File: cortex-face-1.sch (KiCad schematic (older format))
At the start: 12 parts, among them U1 ProMicro

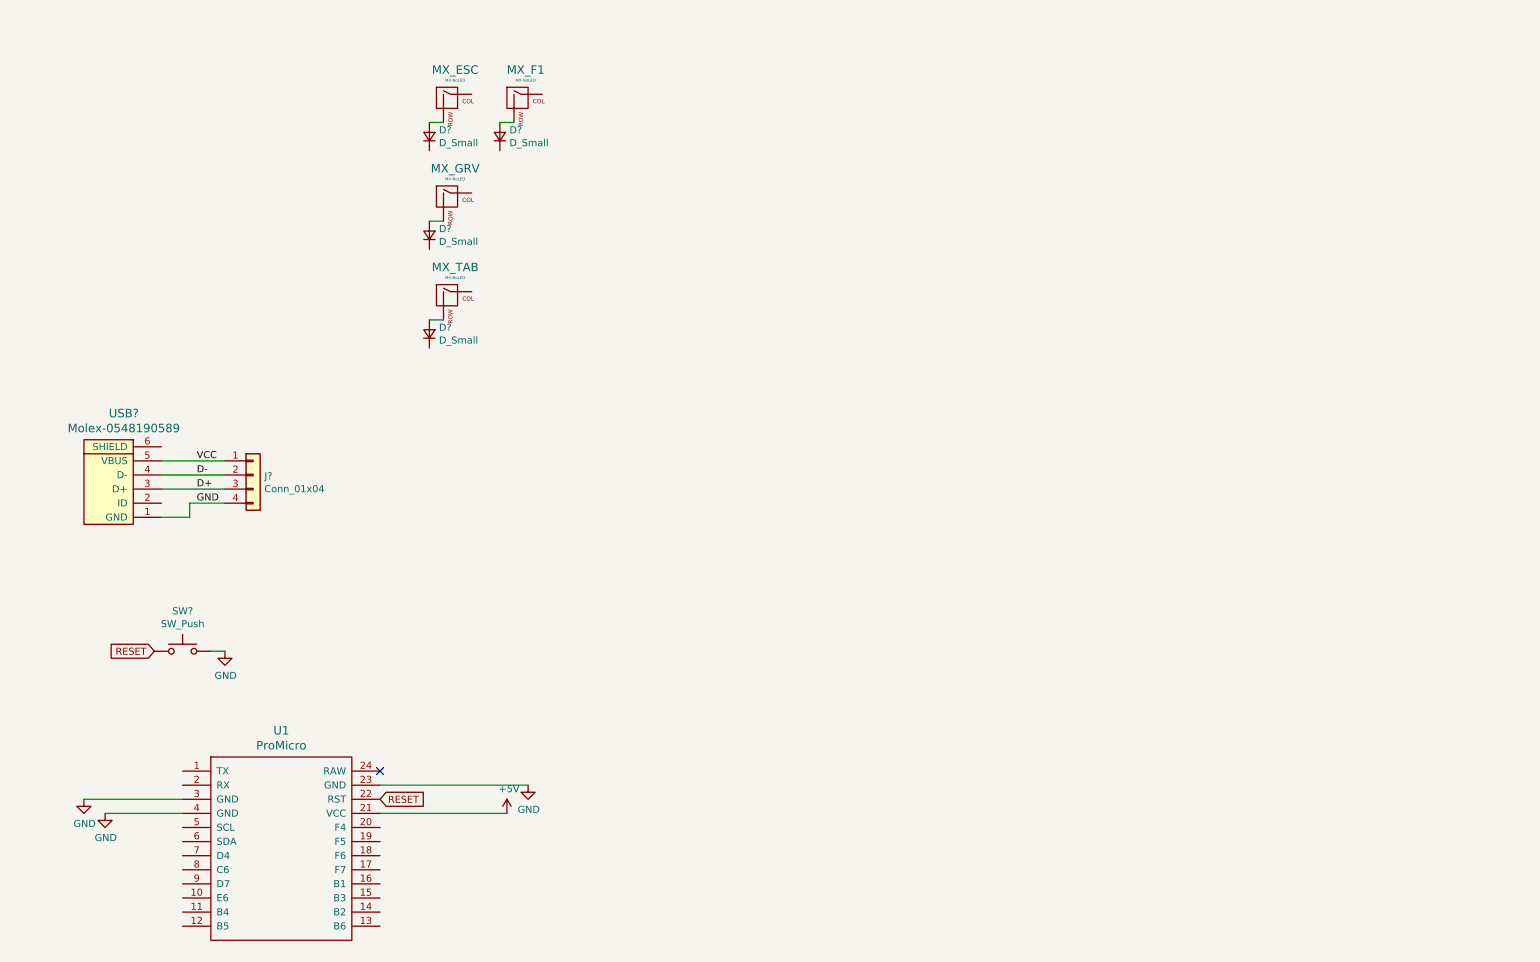
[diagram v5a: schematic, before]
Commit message: 10x9 layout
Changed switch matrix to 10x9 (columns x rows) to use fewer pins
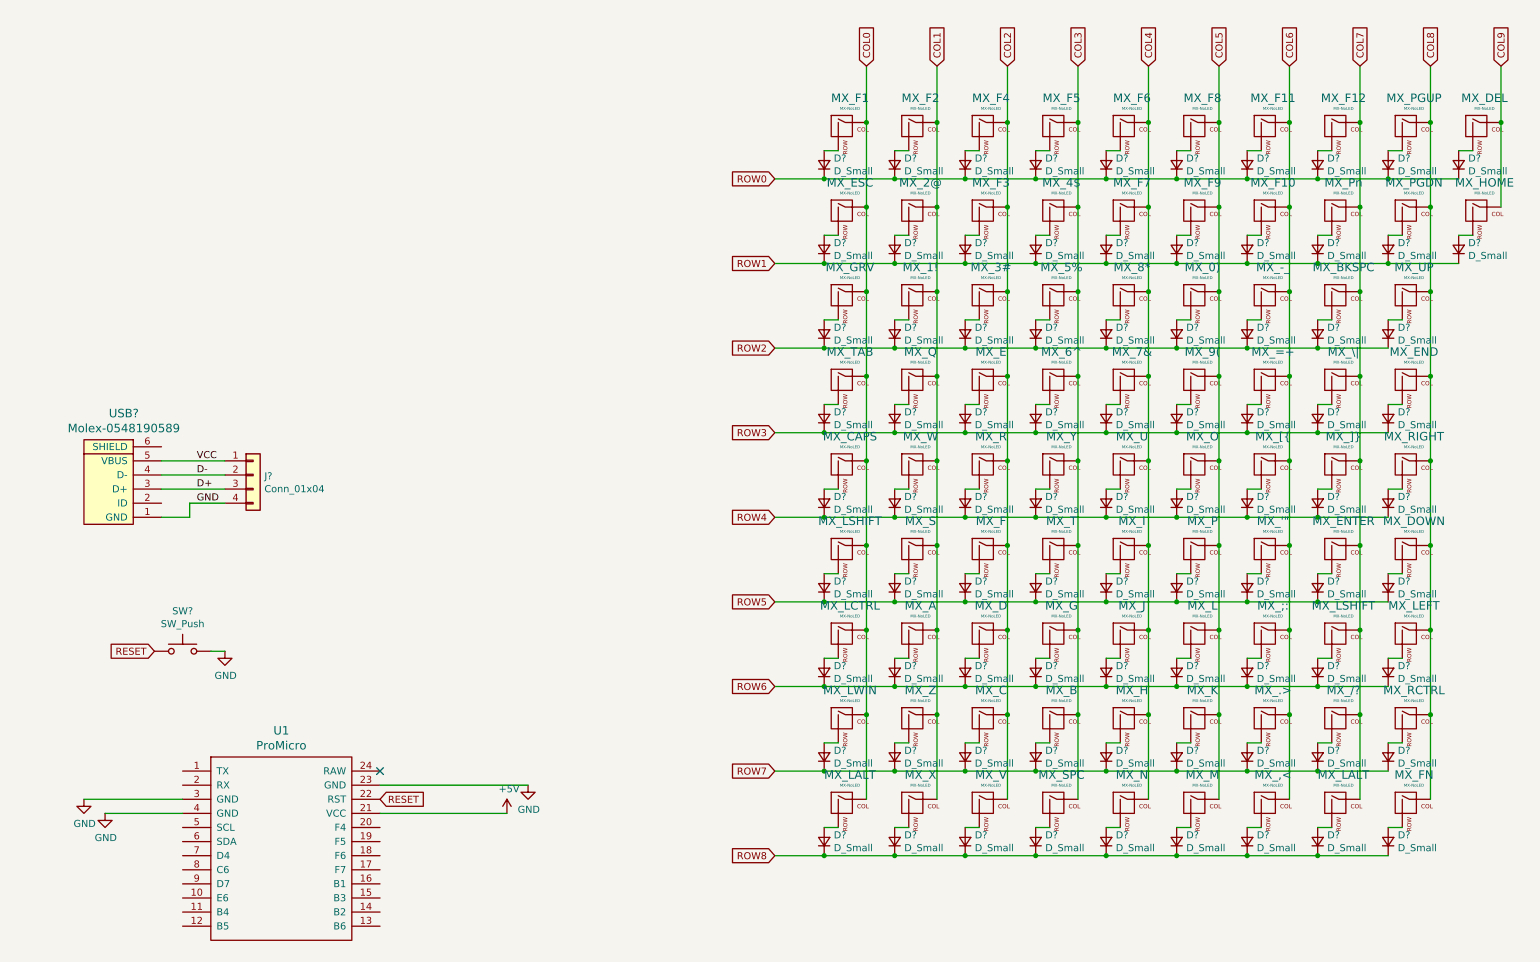
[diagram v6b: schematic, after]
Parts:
- added D? (x79): D_Small, symbol Device:D_Small
- added MX_'", MX_,<, MX_-_, MX_.>, MX_/?, MX_0), MX_1!, MX_2@, MX_3#, MX_4$, MX_5%, MX_6^, MX_7&, MX_8*, MX_9(, MX_;:, MX_=+, MX_A, MX_B, MX_BKSPC, MX_C, MX_CAPS, MX_D, MX_DEL, MX_DOWN, MX_E, MX_END, MX_ENTER, MX_F, MX_F10, MX_F11, MX_F12, MX_F2, MX_F3, MX_F4, MX_F5, MX_F6, MX_F7, MX_F8, MX_F9, MX_FN, MX_G, MX_H, MX_HOME, MX_I, MX_J, MX_K, MX_L, MX_LALT (x2), MX_LCTRL, MX_LEFT, MX_LSHIFT (x2), MX_LWIN, MX_M, MX_N, MX_O, MX_P, MX_PGDN, MX_PGUP, MX_Pn, MX_Q, MX_R, MX_RCTRL, MX_RIGHT, MX_S, MX_SPC, MX_T, MX_U, MX_UP, MX_V, MX_W, MX_X, MX_Y, MX_Z, MX_[{, MX_\|, MX_]}: MX-NoLED, symbol MX_Alps_Hybrid:MX-NoLED
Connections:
- net COL0: now reaches MX_F1.1 (COL)
- net COL0: now also MX_ESC.1 (COL), MX_GRV.1 (COL), MX_TAB.1 (COL), MX_CAPS.1 (COL), MX_LALT.1 (COL), MX_LCTRL.1 (COL), MX_LSHIFT.1 (COL), MX_LWIN.1 (COL)
- net ROW0: now reaches D?.1 (K)
- net ROW0: now also D?.1 (K), D?.1 (K), D?.1 (K), D?.1 (K), D?.1 (K), D?.1 (K), D?.1 (K), D?.1 (K), D?.1 (K)
- net ROW1: now reaches D?.1 (K)
- net ROW1: now also D?.1 (K), D?.1 (K), D?.1 (K), D?.1 (K), D?.1 (K), D?.1 (K), D?.1 (K), D?.1 (K), D?.1 (K)
- net ROW2: now reaches D?.1 (K)
- net ROW2: now also D?.1 (K), D?.1 (K), D?.1 (K), D?.1 (K), D?.1 (K), D?.1 (K), D?.1 (K), D?.1 (K)
- net ROW3: now reaches D?.1 (K)
- net ROW3: now also D?.1 (K), D?.1 (K), D?.1 (K), D?.1 (K), D?.1 (K), D?.1 (K), D?.1 (K), D?.1 (K)
- new net: D?.2 (A), MX_CAPS.2 (ROW)
- new net: D?.2 (A), MX_LSHIFT.2 (ROW) (x2)
- new net: D?.2 (A), MX_LCTRL.2 (ROW)
- new net: D?.2 (A), MX_LWIN.2 (ROW)
- new net: D?.2 (A), MX_LALT.2 (ROW) (x2)
- new net: D?.2 (A), MX_F2.2 (ROW)
- new net: D?.2 (A), MX_2@.2 (ROW)
- new net: D?.2 (A), MX_1!.2 (ROW)
- new net: D?.2 (A), MX_Q.2 (ROW)
- new net: D?.2 (A), MX_W.2 (ROW)
- new net: D?.2 (A), MX_S.2 (ROW)
- new net: D?.2 (A), MX_A.2 (ROW)
- new net: D?.2 (A), MX_Z.2 (ROW)
- new net: D?.2 (A), MX_X.2 (ROW)
- new net: D?.2 (A), MX_F4.2 (ROW)
- new net: D?.2 (A), MX_F3.2 (ROW)
- new net: D?.2 (A), MX_3#.2 (ROW)
- new net: D?.2 (A), MX_E.2 (ROW)
- new net: D?.2 (A), MX_R.2 (ROW)
- new net: D?.2 (A), MX_F.2 (ROW)
- new net: D?.2 (A), MX_D.2 (ROW)
- new net: D?.2 (A), MX_C.2 (ROW)
- new net: D?.2 (A), MX_V.2 (ROW)
- new net: D?.2 (A), MX_F5.2 (ROW)
- new net: D?.2 (A), MX_4$.2 (ROW)
- new net: D?.2 (A), MX_5%.2 (ROW)
- new net: D?.2 (A), MX_6^.2 (ROW)
- new net: D?.2 (A), MX_Y.2 (ROW)
- new net: D?.2 (A), MX_T.2 (ROW)
- new net: D?.2 (A), MX_G.2 (ROW)
- new net: D?.2 (A), MX_B.2 (ROW)
- new net: D?.2 (A), MX_SPC.2 (ROW)
- new net: D?.2 (A), MX_F6.2 (ROW)
- new net: D?.2 (A), MX_F7.2 (ROW)
- new net: D?.2 (A), MX_8*.2 (ROW)
- new net: D?.2 (A), MX_7&.2 (ROW)
- new net: D?.2 (A), MX_U.2 (ROW)
- new net: D?.2 (A), MX_I.2 (ROW)
- new net: D?.2 (A), MX_J.2 (ROW)
- new net: D?.2 (A), MX_H.2 (ROW)
- new net: D?.2 (A), MX_N.2 (ROW)
- new net: D?.2 (A), MX_F8.2 (ROW)
- new net: D?.2 (A), MX_F9.2 (ROW)
- new net: D?.2 (A), MX_0).2 (ROW)
- new net: D?.2 (A), MX_9(.2 (ROW)
- new net: D?.2 (A), MX_O.2 (ROW)
- new net: D?.2 (A), MX_P.2 (ROW)
- new net: D?.2 (A), MX_L.2 (ROW)
- new net: D?.2 (A), MX_K.2 (ROW)
- new net: D?.2 (A), MX_M.2 (ROW)
- new net: D?.2 (A), MX_F11.2 (ROW)
- new net: D?.2 (A), MX_F10.2 (ROW)
- new net: D?.2 (A), MX_-_.2 (ROW)
- new net: D?.2 (A), MX_=+.2 (ROW)
- new net: D?.2 (A), MX_[{.2 (ROW)
- new net: D?.2 (A), MX_'".2 (ROW)
- new net: D?.2 (A), MX_;:.2 (ROW)
- new net: D?.2 (A), MX_.>.2 (ROW)
- new net: D?.2 (A), MX_,<.2 (ROW)
- new net: D?.2 (A), MX_F12.2 (ROW)
- new net: D?.2 (A), MX_Pn.2 (ROW)
- new net: D?.2 (A), MX_BKSPC.2 (ROW)
- new net: D?.2 (A), MX_\|.2 (ROW)
- new net: D?.2 (A), MX_]}.2 (ROW)
- new net: D?.2 (A), MX_ENTER.2 (ROW)
- new net: D?.2 (A), MX_/?.2 (ROW)
- new net: D?.2 (A), MX_PGUP.2 (ROW)
- new net: D?.2 (A), MX_PGDN.2 (ROW)
- new net: D?.2 (A), MX_UP.2 (ROW)
- new net: D?.2 (A), MX_END.2 (ROW)
- new net: D?.2 (A), MX_RIGHT.2 (ROW)
- new net: D?.2 (A), MX_DOWN.2 (ROW)
- new net: D?.2 (A), MX_LEFT.2 (ROW)
- new net: D?.2 (A), MX_RCTRL.2 (ROW)
- new net: D?.2 (A), MX_FN.2 (ROW)
- new net: D?.2 (A), MX_DEL.2 (ROW)
- new net: D?.2 (A), MX_HOME.2 (ROW)
- new net COL1: MX_1!.1 (COL), MX_2@.1 (COL), MX_A.1 (COL), MX_F2.1 (COL), MX_Q.1 (COL), MX_S.1 (COL), MX_W.1 (COL), MX_X.1 (COL), MX_Z.1 (COL)
- new net COL2: MX_3#.1 (COL), MX_C.1 (COL), MX_D.1 (COL), MX_E.1 (COL), MX_F.1 (COL), MX_F3.1 (COL), MX_F4.1 (COL), MX_R.1 (COL), MX_V.1 (COL)
- new net COL3: MX_4$.1 (COL), MX_5%.1 (COL), MX_6^.1 (COL), MX_B.1 (COL), MX_F5.1 (COL), MX_G.1 (COL), MX_SPC.1 (COL), MX_T.1 (COL), MX_Y.1 (COL)
- new net COL4: MX_7&.1 (COL), MX_8*.1 (COL), MX_F6.1 (COL), MX_F7.1 (COL), MX_H.1 (COL), MX_I.1 (COL), MX_J.1 (COL), MX_N.1 (COL), MX_U.1 (COL)
- new net COL5: MX_0).1 (COL), MX_9(.1 (COL), MX_F8.1 (COL), MX_F9.1 (COL), MX_K.1 (COL), MX_L.1 (COL), MX_M.1 (COL), MX_O.1 (COL), MX_P.1 (COL)
- new net COL6: MX_'".1 (COL), MX_,<.1 (COL), MX_-_.1 (COL), MX_.>.1 (COL), MX_;:.1 (COL), MX_=+.1 (COL), MX_F10.1 (COL), MX_F11.1 (COL), MX_[{.1 (COL)
- new net COL7: MX_/?.1 (COL), MX_BKSPC.1 (COL), MX_ENTER.1 (COL), MX_F12.1 (COL), MX_LALT.1 (COL), MX_LSHIFT.1 (COL), MX_Pn.1 (COL), MX_\|.1 (COL), MX_]}.1 (COL)
- new net COL8: MX_DOWN.1 (COL), MX_END.1 (COL), MX_FN.1 (COL), MX_LEFT.1 (COL), MX_PGDN.1 (COL), MX_PGUP.1 (COL), MX_RCTRL.1 (COL), MX_RIGHT.1 (COL), MX_UP.1 (COL)
- new net COL9: MX_DEL.1 (COL), MX_HOME.1 (COL)
- new net ROW4: D?.1 (K), D?.1 (K), D?.1 (K), D?.1 (K), D?.1 (K), D?.1 (K), D?.1 (K), D?.1 (K), D?.1 (K)
- new net ROW5: D?.1 (K), D?.1 (K), D?.1 (K), D?.1 (K), D?.1 (K), D?.1 (K), D?.1 (K), D?.1 (K), D?.1 (K)
- new net ROW6: D?.1 (K), D?.1 (K), D?.1 (K), D?.1 (K), D?.1 (K), D?.1 (K), D?.1 (K), D?.1 (K), D?.1 (K)
- new net ROW7: D?.1 (K), D?.1 (K), D?.1 (K), D?.1 (K), D?.1 (K), D?.1 (K), D?.1 (K), D?.1 (K), D?.1 (K)
- new net ROW8: D?.1 (K), D?.1 (K), D?.1 (K), D?.1 (K), D?.1 (K), D?.1 (K), D?.1 (K), D?.1 (K), D?.1 (K)
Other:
- moved on the sheet: D?, MX_ESC, MX_F1, MX_GRV, MX_TAB

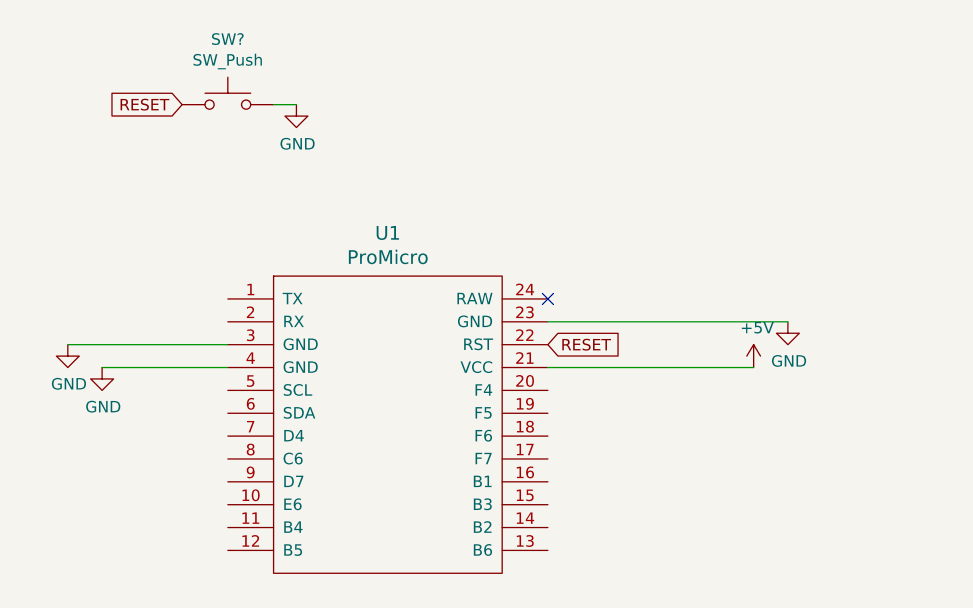
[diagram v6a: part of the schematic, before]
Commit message: Elite-C support
10x9 matrix not supported by Pro Micro, moved to Elite-C instead due to my familiarity and potential for USB-C support in the future. 5 pins left for potential LED support.
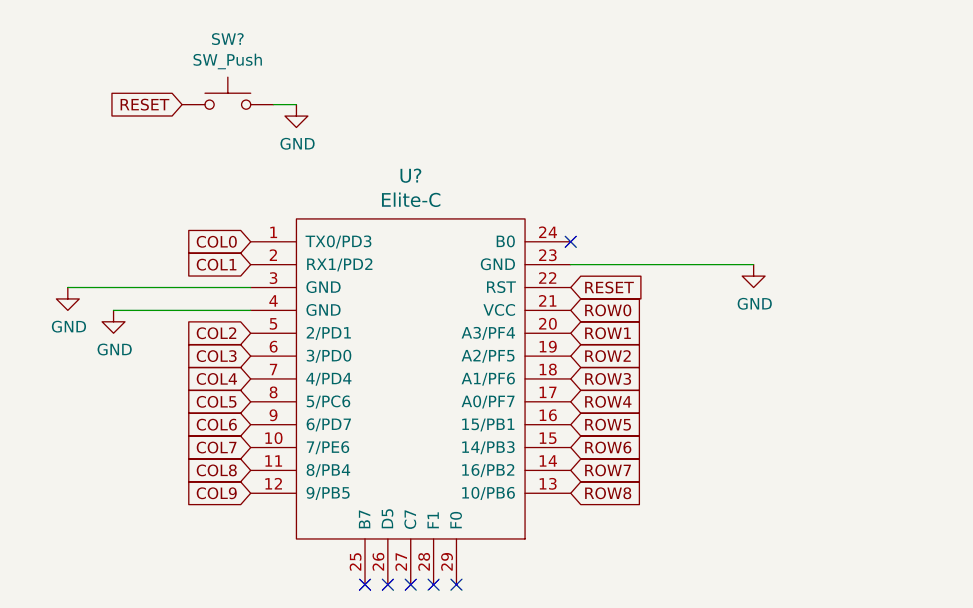
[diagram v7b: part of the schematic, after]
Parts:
- removed U1: ProMicro, symbol promicro:ProMicro
- added U?: Elite-C, symbol keebio:Elite-C
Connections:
- net COL0: now also U?.1 (TX0/PD3)
- net COL1: now also U?.2 (RX1/PD2)
- net COL2: now also U?.5 (2/PD1)
- net COL3: now also U?.6 (3/PD0)
- net COL4: now also U?.7 (4/PD4)
- net COL5: now also U?.8 (5/PC6)
- net COL6: now also U?.9 (6/PD7)
- net COL7: now also U?.10 (7/PE6)
- net COL8: now also U?.11 (8/PB4)
- net COL9: now also U?.12 (9/PB5)
- net GND: now also U?.23 (GND), U?.3 (GND), U?.4 (GND)
- net RESET: now also U?.22 (RST)
- net ROW0: now also U?.21 (VCC)
- net ROW1: now also U?.20 (A3/PF4)
- net ROW2: now also U?.19 (A2/PF5)
- net ROW3: now also U?.18 (A1/PF6)
- net ROW4: now also U?.17 (A0/PF7)
- net ROW5: now also U?.16 (15/PB1)
- net ROW6: now also U?.15 (14/PB3)
- net ROW7: now also U?.14 (16/PB2)
- net ROW8: now also U?.13 (10/PB6)
- no-connect marks 1 -> 6
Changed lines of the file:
@@
 $EndDescr
-$Comp
-L power:GND #PWR0101
-U 1 1 5E172281
-P 1000 6050
-F 0 "#PWR0101" H 1000 5800 50  0001 C CNN
-F 1 "GND" H 1005 5877 50  0000 C CNN
-F 2 "" H 1000 6050 50  0001 C CNN
-F 3 "" H 1000 6050 50  0001 C CNN
-	1    1000 6050
-	1    0    0    -1
-$EndComp
-$Comp
-L power:GND #PWR0103
-U 1 1 5E21C565
-P 4150 5950
-F 0 "#PWR0103" H 4150 5700 50  0001 C CNN
-F 1 "GND" H 4155 5777 50  0000 C CNN
-F 2 "" H 4150 5950 50  0001 C CNN
-F 3 "" H 4150 5950 50  0001 C CNN
-	1    4150 5950
-	1    0    0    -1
-$EndComp
-$Comp
-L power:+5V #PWR?
-U 1 1 5E307ED8
-P 4000 6150
-F 0 "#PWR?" H 4000 6000 50  0001 C CNN
-F 1 "+5V" H 4015 6323 50  0000 C CNN
-F 2 "" H 4000 6150 50  0001 C CNN
-F 3 "" H 4000 6150 50  0001 C CNN
-	1    4000 6150
-	1    0    0    -1
-$EndComp
-Wire Wire Line
-	1000 6050 1700 6050
-$Comp
-L power:GND #PWR?
-U 1 1 5DFB9F5F
-P 1150 6150
-F 0 "#PWR?" H 1150 5900 50  0001 C CNN
-F 1 "GND" H 1155 5977 50  0000 C CNN
-F 2 "" H 1150 6150 50  0001 C CNN
-F 3 "" H 1150 6150 50  0001 C CNN
-	1    1150 6150
-	1    0    0    -1
-$EndComp
-Wire Wire Line
-	1150 6150 1700 6150
-Wire Wire Line
-	3100 5950 4150 5950
-Wire Wire Line
-	3100 6150 4000 6150
 $Comp
 L Switch:SW_Push SW?
@@
 Wire Wire Line
 	2000 5000 1900 5000
-$Comp
-L promicro:ProMicro U1
-U 1 1 5E16F462
-P 2400 6600
-F 0 "U1" H 2400 7637 60  0000 C CNN
-F 1 "ProMicro" H 2400 7531 60  0000 C CNN
-F 2 "" H 2500 5550 60  0000 C CNN
-F 3 "" H 2500 5550 60  0000 C CNN
-	1    2400 6600
-	1    0    0    -1
-$EndComp
-Text GLabel 3100 6050 2    50   Input ~ 0
-RESET
 Text GLabel 1500 5000 0    50   Input ~ 0
 RESET
@@
 Text Label 1800 3950 0    50   ~ 0
 GND
-NoConn ~ 3100 5850
 Text GLabel 11050 850  1    50   Input ~ 0
 COL9
@@
 Wire Wire Line
 	11050 850  11050 1250
+$Comp
+L keebio:Elite-C U?
+U 1 1 5DFC593F
+P 2500 6150
+F 0 "U?" H 2500 6987 60  0000 C CNN
+F 1 "Elite-C" H 2500 6881 60  0000 C CNN
+F 2 "" V 3550 3650 60  0001 C CNN
+F 3 "" V 3550 3650 60  0001 C CNN
+	1    2500 6150
+	1    0    0    -1
+$EndComp
+NoConn ~ 3200 5600
+Text GLabel 3200 5900 2    50   Input ~ 0
+ROW0
+$Comp
+L power:GND #PWR?
+U 1 1 5DFDE84B
+P 1000 5800
+F 0 "#PWR?" H 1000 5550 50  0001 C CNN
+F 1 "GND" H 1005 5627 50  0000 C CNN
+F 2 "" H 1000 5800 50  0001 C CNN
+F 3 "" H 1000 5800 50  0001 C CNN
+	1    1000 5800
+	1    0    0    -1
+$EndComp
+Wire Wire Line
+	1800 5800 1000 5800
+$Comp
+L power:GND #PWR?
+U 1 1 5DFF615E
+P 1200 5900
+F 0 "#PWR?" H 1200 5650 50  0001 C CNN
+F 1 "GND" H 1205 5727 50  0000 C CNN
+F 2 "" H 1200 5900 50  0001 C CNN
+F 3 "" H 1200 5900 50  0001 C CNN
+	1    1200 5900
+	1    0    0    -1
+$EndComp
+Wire Wire Line
+	1200 5900 1800 5900
+Text GLabel 3200 6100 2    50   Input ~ 0
+ROW2
+Text GLabel 3200 6200 2    50   Input ~ 0
+ROW3
+Text GLabel 3200 6300 2    50   Input ~ 0
+ROW4
+Text GLabel 3200 6400 2    50   Input ~ 0
+ROW5
+Text GLabel 3200 6500 2    50   Input ~ 0
+ROW6
+Text GLabel 3200 5800 2    50   Input ~ 0
+RESET
+Text GLabel 3200 6600 2    50   Input ~ 0
+ROW7
+Text GLabel 3200 6700 2    50   Input ~ 0
+ROW8
+$Comp
+L power:GND #PWR?
+U 1 1 5E0176F9
+P 4000 5700
+F 0 "#PWR?" H 4000 5450 50  0001 C CNN
+F 1 "GND" H 4005 5527 50  0000 C CNN
+F 2 "" H 4000 5700 50  0001 C CNN
+F 3 "" H 4000 5700 50  0001 C CNN
+	1    4000 5700
+	1    0    0    -1
+$EndComp
+Wire Wire Line
+	4000 5700 3200 5700
+Text GLabel 3200 6000 2    50   Input ~ 0
+ROW1
+Text GLabel 1800 5600 0    50   Input ~ 0
+COL0
+Text GLabel 1800 5700 0    50   Input ~ 0
+COL1
+Text GLabel 1800 6000 0    50   Input ~ 0
+COL2
+Text GLabel 1800 6100 0    50   Input ~ 0
+COL3
+Text GLabel 1800 6200 0    50   Input ~ 0
+COL4
+Text GLabel 1800 6300 0    50   Input ~ 0
+COL5
+Text GLabel 1800 6400 0    50   Input ~ 0
+COL6
+Text GLabel 1800 6500 0    50   Input ~ 0
+COL7
+Text GLabel 1800 6600 0    50   Input ~ 0
+COL8
+Text GLabel 1800 6700 0    50   Input ~ 0
+COL9
+NoConn ~ 2300 7100
+NoConn ~ 2400 7100
+NoConn ~ 2500 7100
+NoConn ~ 2600 7100
+NoConn ~ 2700 7100
 $EndSCHEMATC
